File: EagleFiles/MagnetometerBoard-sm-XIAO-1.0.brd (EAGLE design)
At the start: 48.4 x 45.6 mm, 10 parts

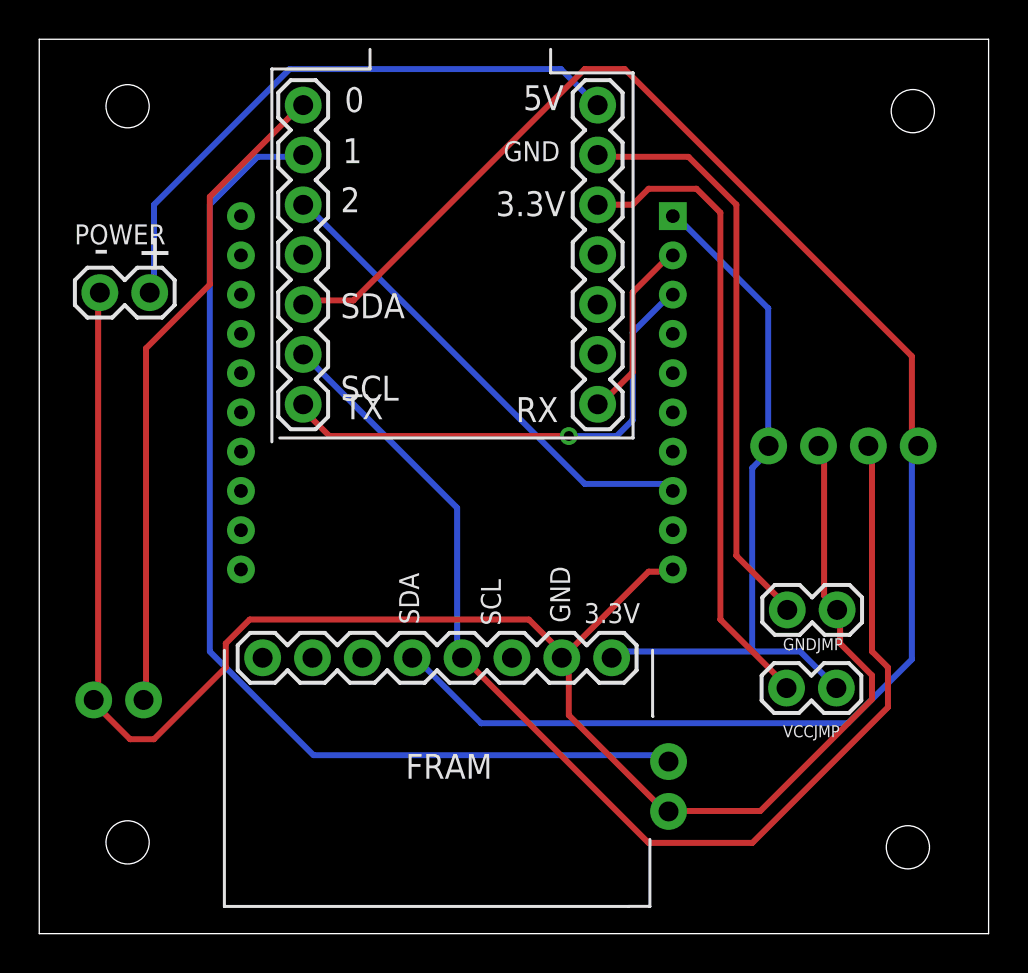
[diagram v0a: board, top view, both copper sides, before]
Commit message: 2ND ORDER PCBWAY
FRAM ORIANTATION AND CONNECTIONS FIXED
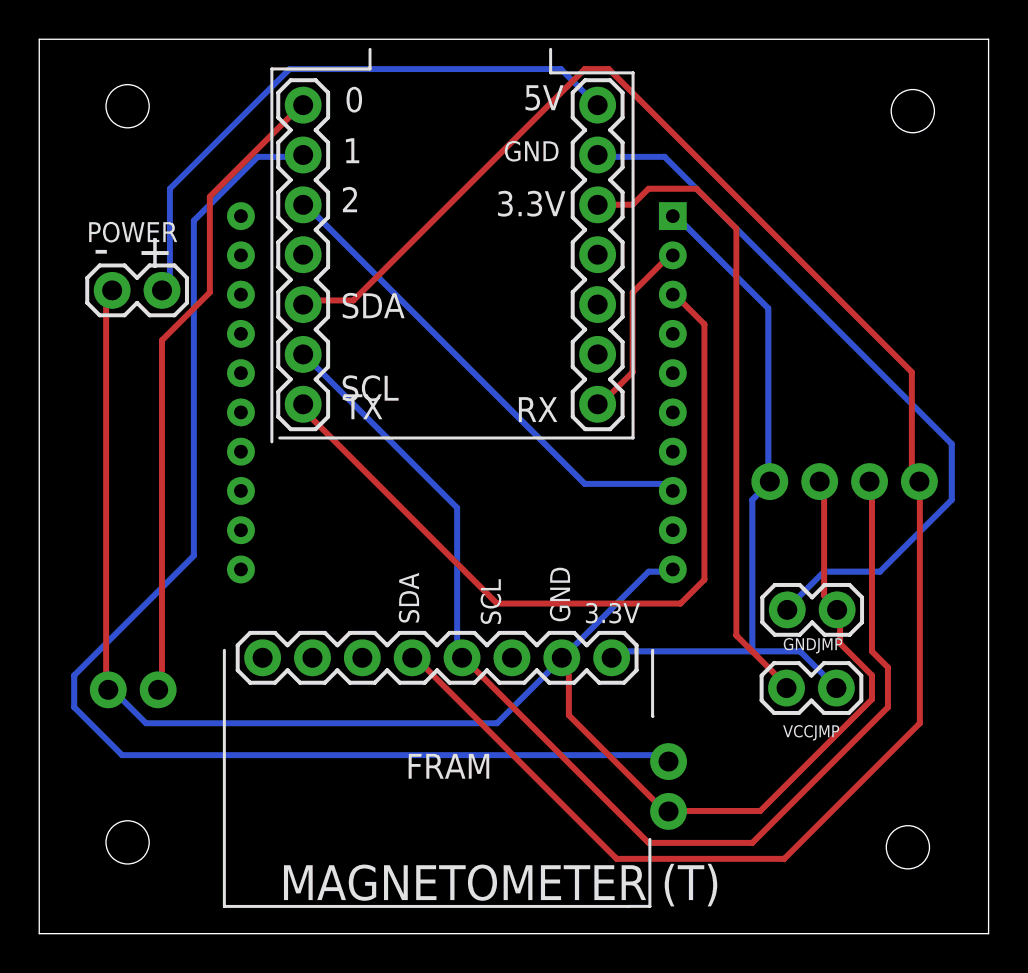
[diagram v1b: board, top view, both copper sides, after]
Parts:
- moved MAGT 1.82 mm to (34.2, 29.4)
- moved LED 0.90 mm to (3.06, 18.8)
- moved POWER 0.64 mm to (3.25, 39.1)
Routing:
- net N$3: track 25.4 -> 40.5 mm, vias 1 -> 0
- net N$11: track 54.3 -> 65.7 mm
- net N$8: track 29.8 -> 37.7 mm
- net N$7: track 86.1 -> 93.4 mm
- net GND: track 94.5 -> 88.6 mm
- net N$6: track 60.9 -> 59.1 mm
- net N$10: track 33.7 -> 32.9 mm
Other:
- board text added: "MAGNETOMETER (B)"
- board text added: "MAGNETOMETER (T)"
